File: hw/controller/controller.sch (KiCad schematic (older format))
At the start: 71 parts, among them P1 USB_OTG, P10 GPIO, P11 VDD_SEL, P12 UART0, P13 SPI, P14 I2C0, P15 I2C1, P16 I2C2, P17 I2C3, P18 I2C4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

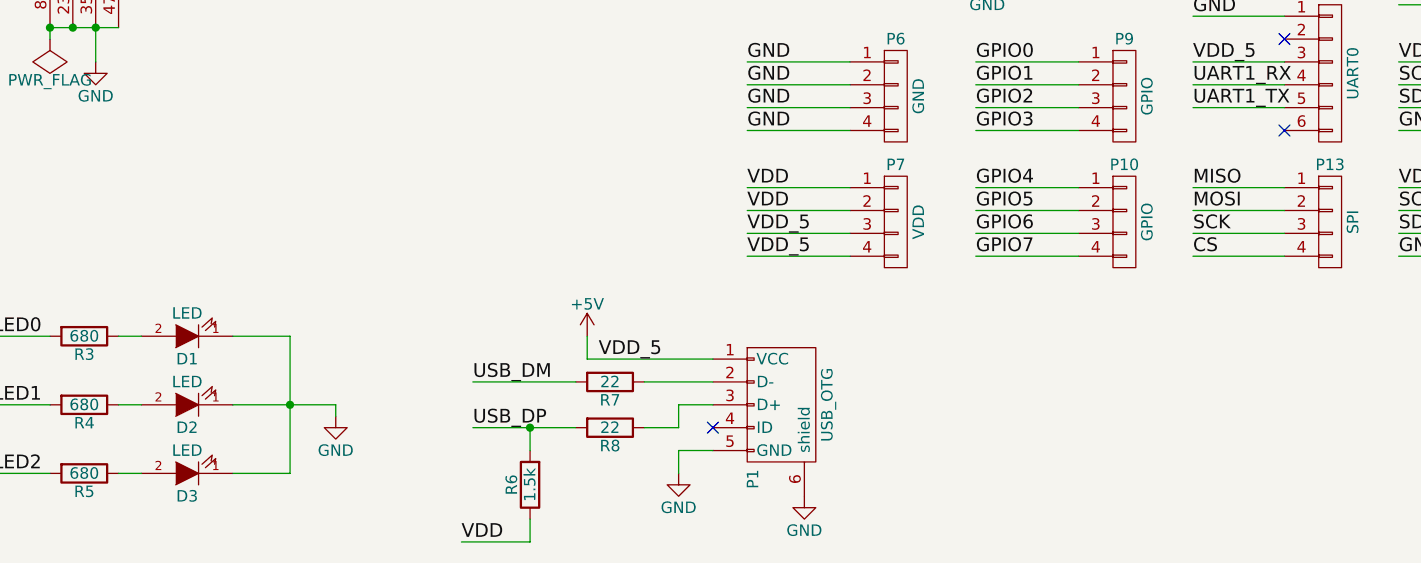
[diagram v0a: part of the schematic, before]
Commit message: Placement mostly done and half routed
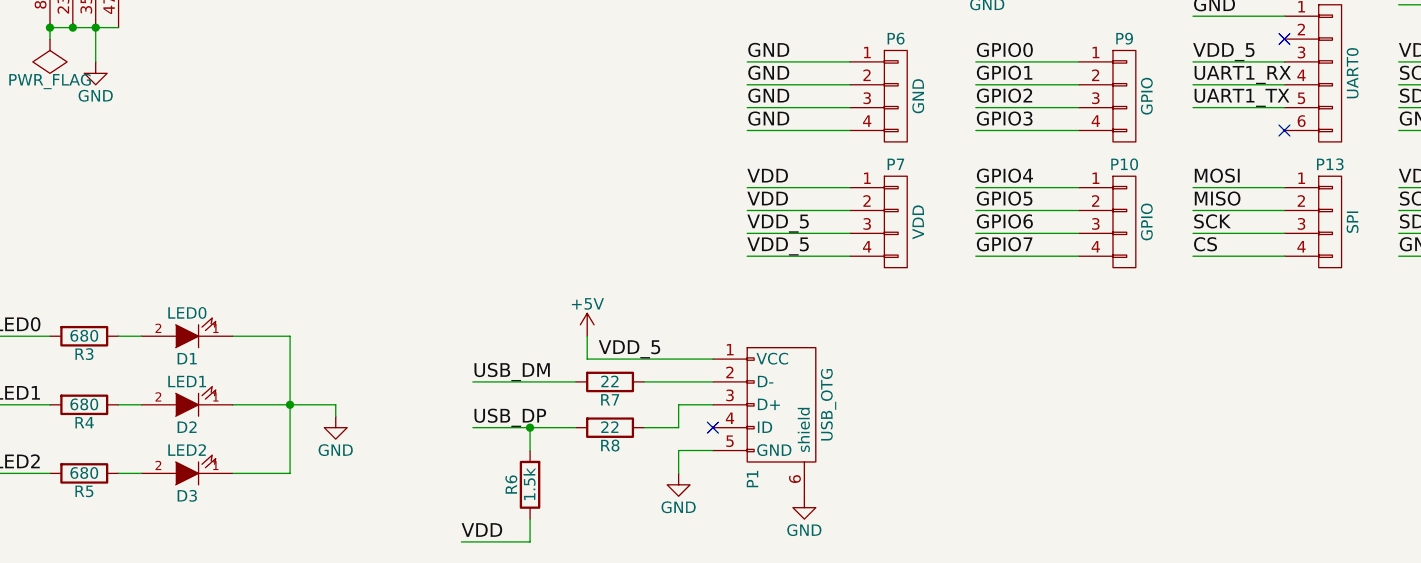
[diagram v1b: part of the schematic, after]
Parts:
- D1: value LED -> LED0
- D2: value LED -> LED1
- D3: value LED -> LED2
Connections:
- net MISO: now also P13.2 (P2); no longer P13.1 (P1)
- net MOSI: now also P13.1 (P1); no longer P13.2 (P2)
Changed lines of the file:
@@
 P 3600 7150
 F 0 "D3" H 3600 7250 50  0000 C CNN
-F 1 "LED" H 3600 7050 50  0000 C CNN
+F 1 "LED2" H 3600 7050 50  0000 C CNN
 F 2 "LEDs:LED_0805" H 3600 7150 50  0001 C CNN
 F 3 "" H 3600 7150 50  0000 C CNN
@@
 P 3600 6850
 F 0 "D2" H 3600 6950 50  0000 C CNN
-F 1 "LED" H 3600 6750 50  0000 C CNN
+F 1 "LED1" H 3600 6750 50  0000 C CNN
 F 2 "LEDs:LED_0805" H 3600 6850 50  0001 C CNN
 F 3 "" H 3600 6850 50  0000 C CNN
@@
 P 3600 6550
 F 0 "D1" H 3600 6650 50  0000 C CNN
-F 1 "LED" H 3600 6450 50  0000 C CNN
+F 1 "LED0" H 3600 6450 50  0000 C CNN
 F 2 "LEDs:LED_0805" H 3600 6550 50  0001 C CNN
 F 3 "" H 3600 6550 50  0000 C CNN
@@
 $EndComp
 Text Label 8000 5900 0    60   ~ 0
+MOSI
+Text Label 8000 6000 0    60   ~ 0
 MISO
-Text Label 8000 6000 0    60   ~ 0
-MOSI
 Text Label 8000 6100 0    60   ~ 0
 SCK

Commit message: Ostur Controller Layout 1.0 done!
I think...
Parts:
- SW1, SW2: footprint (none) -> footprints:PTS645SM43SMTR92
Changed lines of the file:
@@
 F 0 "SW1" H 1850 6460 50  0000 C CNN
 F 1 "RST" H 1700 6270 50  0000 C CNN
-F 2 "" H 1700 6350 50  0001 C CNN
+F 2 "footprints:PTS645SM43SMTR92" H 1700 6350 50  0001 C CNN
 F 3 "" H 1700 6350 50  0000 C CNN
 	1    1700 6350
@@
 F 0 "SW2" H 1850 6860 50  0000 C CNN
 F 1 "BOOT" H 1700 6670 50  0000 C CNN
-F 2 "" H 1700 6750 50  0001 C CNN
+F 2 "footprints:PTS645SM43SMTR92" H 1700 6750 50  0001 C CNN
 F 3 "" H 1700 6750 50  0000 C CNN
 	1    1700 6750

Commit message: Updated part numbers for controller
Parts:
- C1: mpn (none) -> CL21B103KBANNNC
- C2: mpn (none) -> CL21C220JBANNNC
- C5: mpn (none) -> CL21B104MBCNNNC
- P1: mpn (none) -> 10118192-0001LF
- R1: mpn (none) -> RC0805JR-07390RL
- R3: mpn (none) -> RC0805JR-07680RL
- R6: mpn (none) -> RC0805JR-071K5L
- R7: mpn (none) -> RC0805JR-0722RL
- R9: mpn (none) -> 311-10KARCT-ND
- SW1: mpn (none) -> PTS645SM43SMTR92
- U1: mpn (none) -> STM32F072CBT6
- U2: mpn (none) -> LD1117S33CTR
- U3: mpn (none) -> TCA9548APWR
- Y1: mpn (none) -> CTX1055CT-ND
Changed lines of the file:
@@
 F 2 "footprints:LQFP48" H 2000 2700 60  0001 C CNN
 F 3 "" H 2000 2700 60  0000 C CNN
+F 4 "STM32F072CBT6" H 2000 2700 60  0001 C CNN "mpn"
 	1    2000 2700
 	1    0    0    -1
@@
 F 2 "Housings_SSOP:TSSOP-24_4.4x7.8mm_Pitch0.65mm" H 6150 1350 60  0001 C CNN
 F 3 "" H 6150 1350 60  0000 C CNN
+F 4 "TCA9548APWR" H 6150 1350 60  0001 C CNN "mpn"
 	1    6150 1350
 	1    0    0    -1
@@
 F 2 "Resistors_SMD:R_0805" V 1430 2800 50  0001 C CNN
 F 3 "" H 1500 2800 50  0000 C CNN
+F 4 "RC0805JR-07390RL" V 1500 2800 60  0001 C CNN "mpn"
 	1    1500 2800
 	0    1    1    0
@@
 F 2 "footprints:ATS-SM-CRYSTAL" H 1100 2600 50  0001 C CNN
 F 3 "" H 1100 2600 50  0000 C CNN
+F 4 "CTX1055CT-ND" H 1100 2600 60  0001 C CNN "mpn"
 	1    1100 2600
 	0    1    1    0
@@
 F 2 "Capacitors_SMD:C_0805" H 900 2400 50  0001 C CNN
 F 3 "" H 900 2400 50  0000 C CNN
+F 4 "CL21C220JBANNNC" H 900 2400 60  0001 C CNN "mpn"
 	1    900  2400
 	0    1    1    0
@@
 F 2 "Capacitors_SMD:C_0805" H 1700 1250 50  0001 C CNN
 F 3 "" H 1700 1250 50  0000 C CNN
+F 4 "CL21B104MBCNNNC" H 1700 1250 60  0001 C CNN "mpn"
 	1    1700 1250
 	1    0    0    -1
@@
 F 2 "footprints:PTS645SM43SMTR92" H 1700 6350 50  0001 C CNN
 F 3 "" H 1700 6350 50  0000 C CNN
+F 4 "PTS645SM43SMTR92" H 1700 6350 60  0001 C CNN "mpn"
 	1    1700 6350
 	1    0    0    -1
@@
 F 2 "Capacitors_SMD:C_0805" H 1200 1250 50  0001 C CNN
 F 3 "" H 1200 1250 50  0000 C CNN
+F 4 "CL21B103KBANNNC" H 1200 1250 60  0001 C CNN "mpn"
 	1    1200 1250
 	1    0    0    -1
@@
 F 2 "Resistors_SMD:R_0805" V 3080 6550 50  0001 C CNN
 F 3 "" H 3150 6550 50  0000 C CNN
+F 4 "RC0805JR-07680RL" V 3150 6550 60  0001 C CNN "mpn"
 	1    3150 6550
 	0    1    1    0
@@
 F 2 "footprints:USB_MICRO_B" V 6150 6750 50  0001 C CNN
 F 3 "" V 6150 6750 50  0000 C CNN
+F 4 "10118192-0001LF" H 6200 6850 60  0001 C CNN "mpn"
 	1    6200 6850
 	0    1    1    0
@@
 F 2 "Resistors_SMD:R_0805" V 5380 6750 50  0001 C CNN
 F 3 "" H 5450 6750 50  0000 C CNN
+F 4 "RC0805JR-0722RL" V 5450 6750 60  0001 C CNN "mpn"
 	1    5450 6750
 	0    1    1    0
@@
 F 2 "Resistors_SMD:R_0805" V 5030 7200 50  0001 C CNN
 F 3 "" H 5100 7200 50  0000 C CNN
+F 4 "RC0805JR-071K5L" V 5100 7200 60  0001 C CNN "mpn"
 	1    5100 7200
 	-1   0    0    1
@@
 F 2 "footprints:SOT-223" H 4200 1250 50  0001 C CNN
 F 3 "" H 4200 1150 50  0000 C CNN
+F 4 "LD1117S33CTR" H 4200 1150 60  0001 C CNN "mpn"
 	1    4200 1150
 	1    0    0    -1
@@
 F 2 "Resistors_SMD:R_0805" V 9930 850 50  0001 C CNN
 F 3 "" H 10000 850 50  0000 C CNN
+F 4 "311-10KARCT-ND" V 10000 850 60  0001 C CNN "mpn"
 	1    10000 850
 	0    -1   -1   0

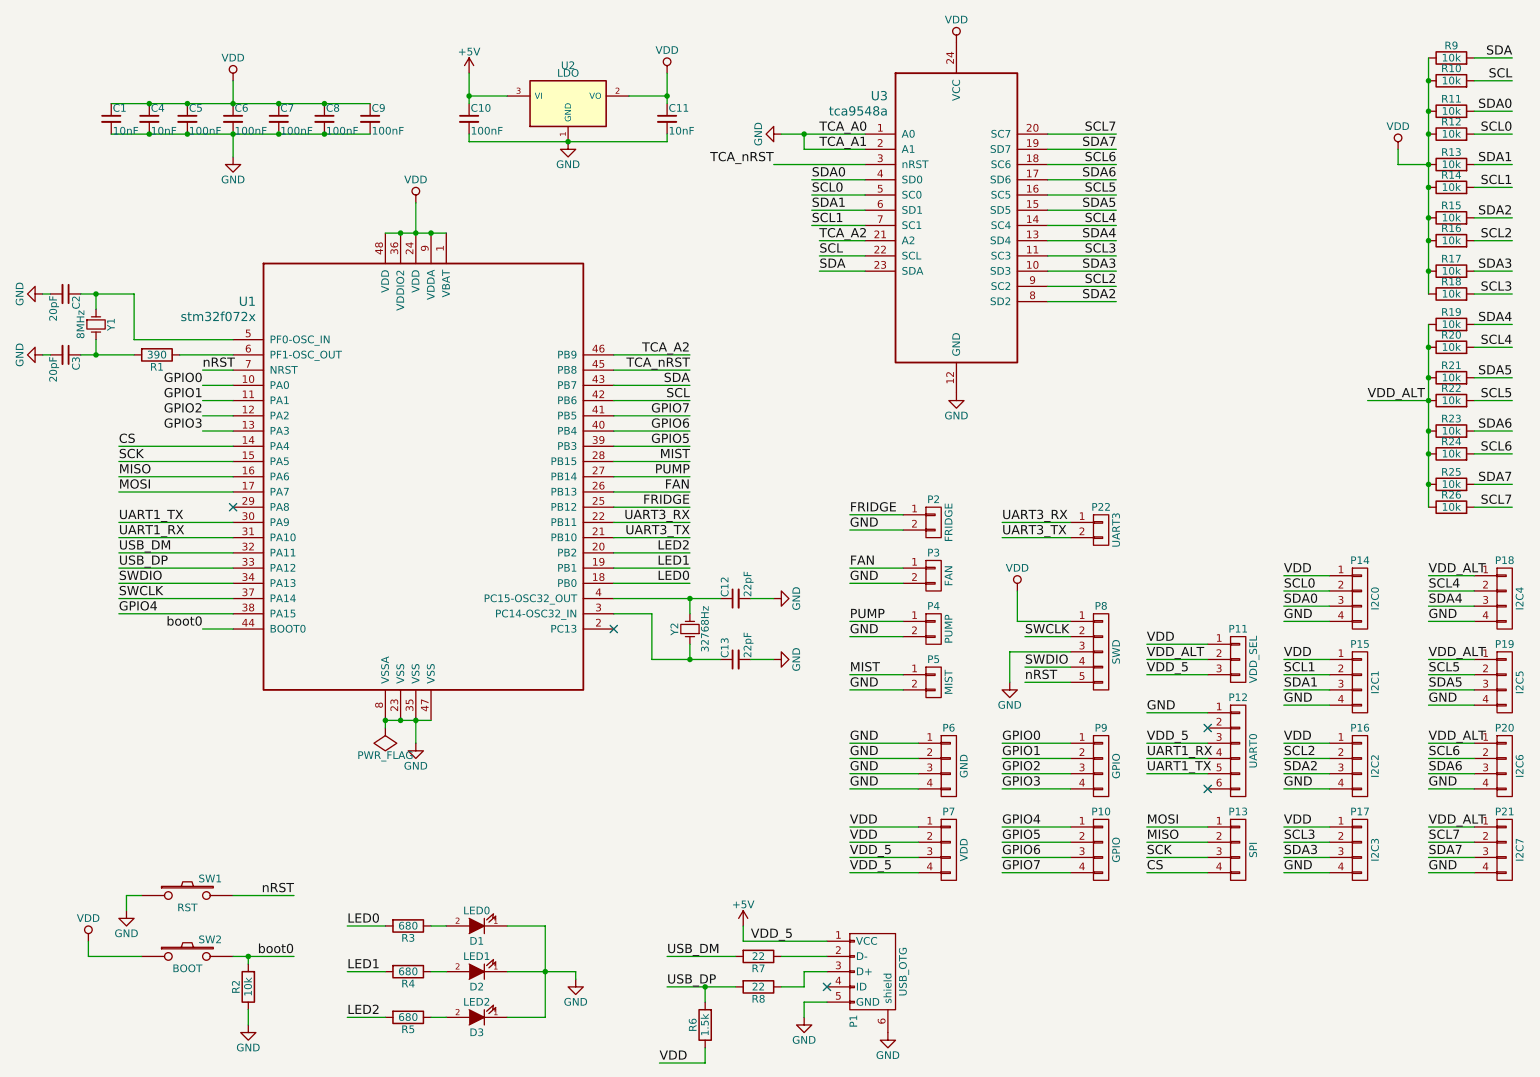
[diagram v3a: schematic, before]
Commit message: Updated ostur controller to v1.1
Some changes:
Reduced i2c to 4 channels instead of 8
Added ARM-SWD 10-pin connector
Removed 8MHz crystal (not needed for usb)
Added actual footprint for 32.768kHz crystal
Moved uart, not sure why though...
Smaller board!
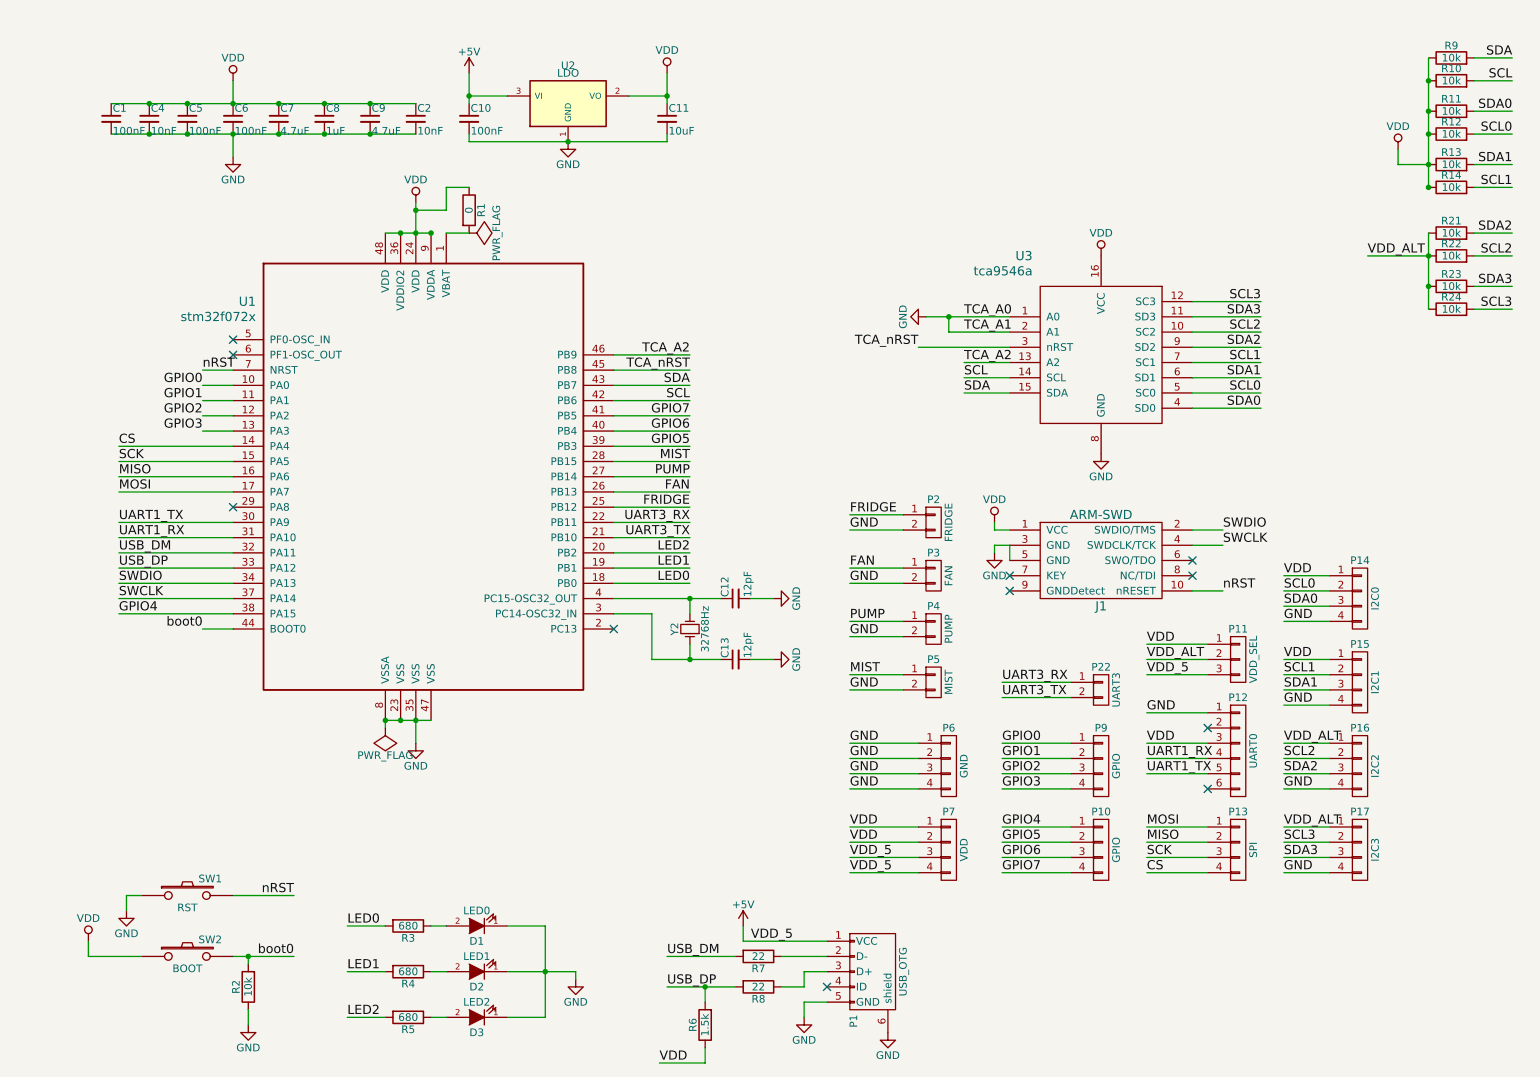
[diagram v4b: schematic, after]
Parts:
- removed C3: 20pF, Capacitors_SMD:C_0805, symbol C_Small
- removed P18: I2C4, Pin_Headers:Pin_Header_Straight_1x04, symbol CONN_01X04
- removed P19: I2C5, Pin_Headers:Pin_Header_Straight_1x04, symbol CONN_01X04
- removed P20: I2C6, Pin_Headers:Pin_Header_Straight_1x04, symbol CONN_01X04
- removed P21: I2C7, Pin_Headers:Pin_Header_Straight_1x04, symbol CONN_01X04
- removed P8: SWD, Pin_Headers:Pin_Header_Straight_1x05, symbol CONN_01X05
- removed R15, R16, R17, R18, R19, R20, R25, R26: 10k, Resistors_SMD:R_0805, symbol R
- removed U3: tca9548a, Housings_SSOP:TSSOP-24_4.4x7.8mm_Pitch0.65mm, symbol tca9548a
- removed Y1: 8MHz, footprints:ATS-SM-CRYSTAL, symbol Crystal_Small
- added J1: ARM-SWD, footprints:ARM_SWD_SMD, symbol ARM-SWD
- added U3: tca9546a, Housings_SSOP:TSSOP-16_4.4x5mm_Pitch0.65mm, symbol tca9546a
- C1: value 10nF -> 100nF
- C11: value 10nF -> 10uF
- C12, C13: value 22pF -> 12pF; footprint Capacitors_SMD:C_0805 -> Capacitors_SMD:C_0603
- C2: value 20pF -> 10nF; mpn CL21C220JBANNNC -> (none)
- C7, C9: value 100nF -> 4.7uF
- C8: value 100nF -> 1uF
- R1: value 390 -> 0; mpn RC0805JR-07390RL -> (none)
- Y2: footprint footprints:ATS-SM-CRYSTAL -> footprints:FC-135
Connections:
- net SCL5 is gone; now on net SCL2: R22.2
- net SCL6 is gone; now on net SCL3: R24.2
- net SDA5 is gone; now on net SDA2: R21.2
- net SDA6 is gone; now on net SDA3: R23.2
- net +5V: no longer P12.3 (P3)
- net GND: now also J1.3 (GND), J1.5 (GND), U3.1 (A0), U3.2 (A1), U3.8 (GND)
- net SCL: now also U3.14 (SCL)
- net SCL0: now also U3.5 (SC0)
- net SCL1: now also U3.7 (SC1)
- net SCL2: now also U3.10 (SC2)
- net SCL3: now also U3.12 (SC3)
- net SDA: now also U3.15 (SDA)
- net SDA0: now also U3.4 (SD0)
- net SDA1: now also U3.6 (SD1)
- net SDA2: now also U3.9 (SD2)
- net SDA3: now also U3.11 (SD3)
- net SWCLK: now also J1.4 (SWDCLK/TCK)
- net SWDIO: now also J1.2 (SWDIO/TMS)
- net TCA_A2: now also U3.13 (A2)
- net TCA_nRST: now also U3.3 (nRST)
- net VDD: now also C2.1, P12.3 (P3), R1.1, J1.1 (VCC), U3.16 (VCC); no longer P16.1 (P1), P17.1 (P1), U1.1 (VBAT)
- net VDD_ALT: now also P16.1 (P1), P17.1 (P1)
- net nRST: now also J1.10 (nRESET)
- net at U1.5 (PF0-OSC_IN): no longer C2.1
- net at U1.6 (PF1-OSC_OUT): no longer R1.1
- net at R1.2: now also U1.1 (VBAT)
- no-connect marks 5 -> 11
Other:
- moved on the sheet: P22, R21, R22, R23, R24
